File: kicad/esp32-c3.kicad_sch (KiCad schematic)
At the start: 19 parts, among them U1 SN65HVD230, U2 SN65HVD75, U5 ESP32-C3-MINI-1

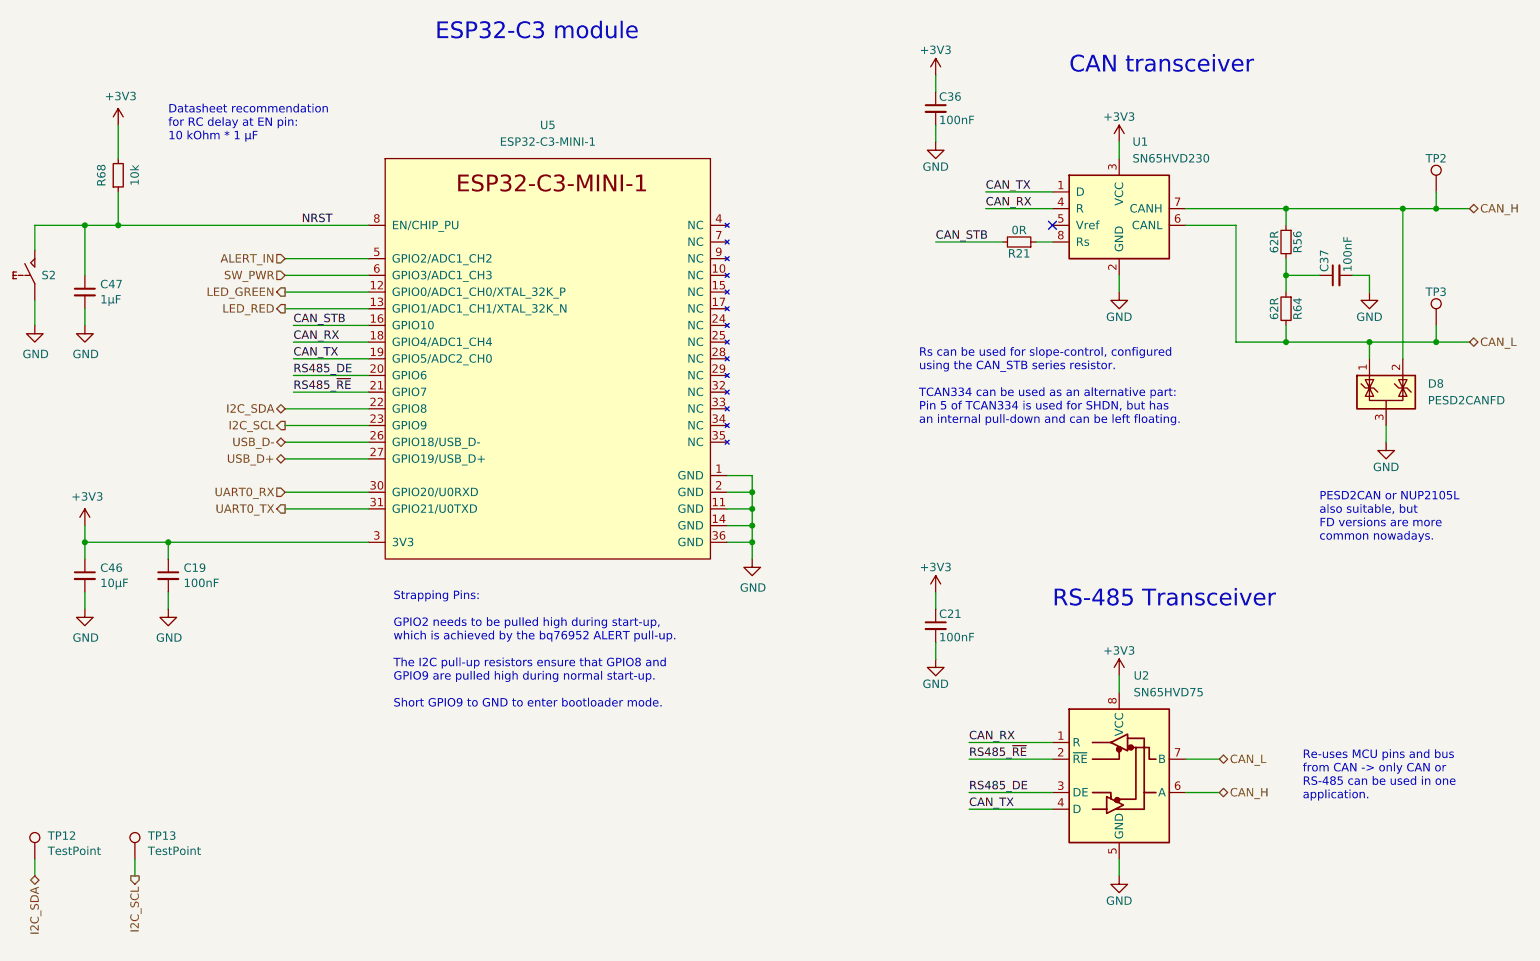
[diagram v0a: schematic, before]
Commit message: Create cost-optimized Lite variant of the BMS C1 v0.4.1
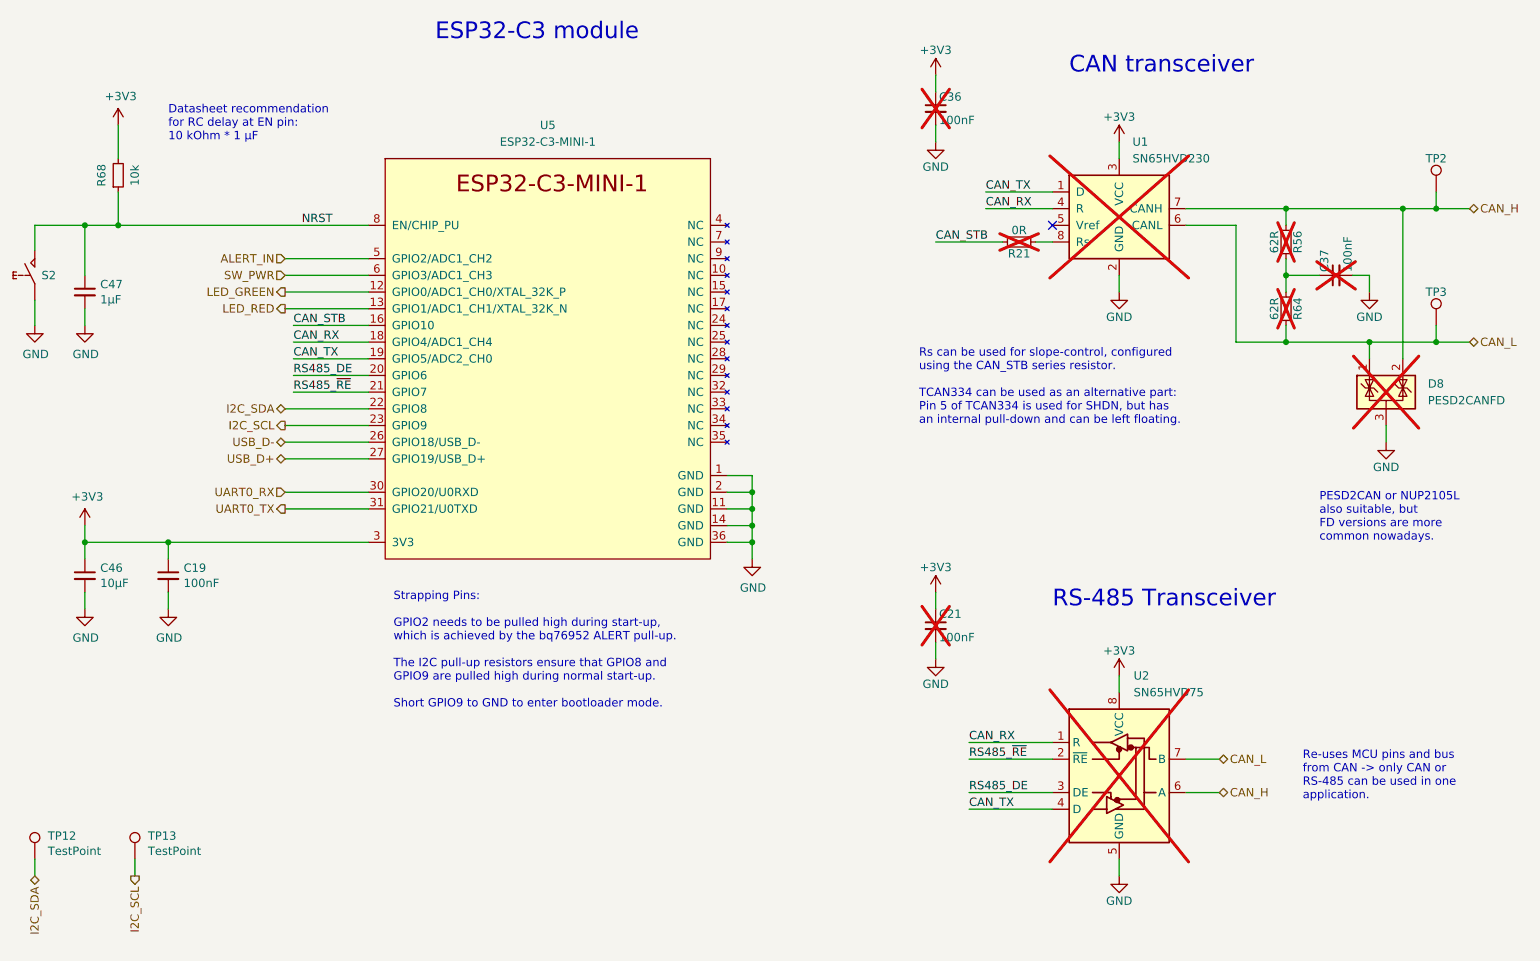
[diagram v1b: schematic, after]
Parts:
- C21, C36, C37, D8, R21, R56, R64, U1, U2: now not fitted
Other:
- title: Libre Solar BMS C1 -> Libre Solar BMS C1 lite
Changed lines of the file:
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@@
 	(paper "A4")
 	(title_block
-		(title "Libre Solar BMS C1")
+		(title "Libre Solar BMS C1 lite")
 		(date "2024-03-17")
 		(rev "0.4.1")
@@
 		(in_bom yes)
 		(on_board yes)
-		(dnp no)
+		(dnp yes)
 		(property "Reference" "C37"
 			(at 236.982 65.532 0)
@@
 		(in_bom yes)
 		(on_board yes)
-		(dnp no)
+		(dnp yes)
 		(property "Reference" "R56"
 			(at 232.918 60.96 90)
@@
 		(in_bom yes)
 		(on_board yes)
-		(dnp no)
+		(dnp yes)
 		(property "Reference" "C36"
 			(at 178.308 38.862 0)
@@
 		(in_bom yes)
 		(on_board yes)
-		(dnp no)
+		(dnp yes)
 		(fields_autoplaced yes)
 		(property "Reference" "U2"
@@
 		(in_bom yes)
 		(on_board yes)
-		(dnp no)
+		(dnp yes)
 		(fields_autoplaced yes)
 		(property "Reference" "D8"
@@
 		(in_bom yes)
 		(on_board yes)
-		(dnp no)
+		(dnp yes)
 		(property "Reference" "C21"
 			(at 178.308 117.602 0)
@@
 		(in_bom yes)
 		(on_board yes)
-		(dnp no)
+		(dnp yes)
 		(property "Reference" "R64"
 			(at 232.918 71.12 90)
@@
 		(in_bom yes)
 		(on_board yes)
-		(dnp no)
+		(dnp yes)
 		(fields_autoplaced yes)
 		(property "Reference" "U1"
@@
 		(in_bom yes)
 		(on_board yes)
-		(dnp no)
+		(dnp yes)
 		(property "Reference" "R21"
 			(at 190.5 62.738 90)
